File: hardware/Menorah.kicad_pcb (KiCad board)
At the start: 2 copper layers, 111.6 x 130.3 mm, 32 parts, among them J1 Conn_02x03_Odd_Even, SW1 SW_Push, U1 ATtiny85-20PU

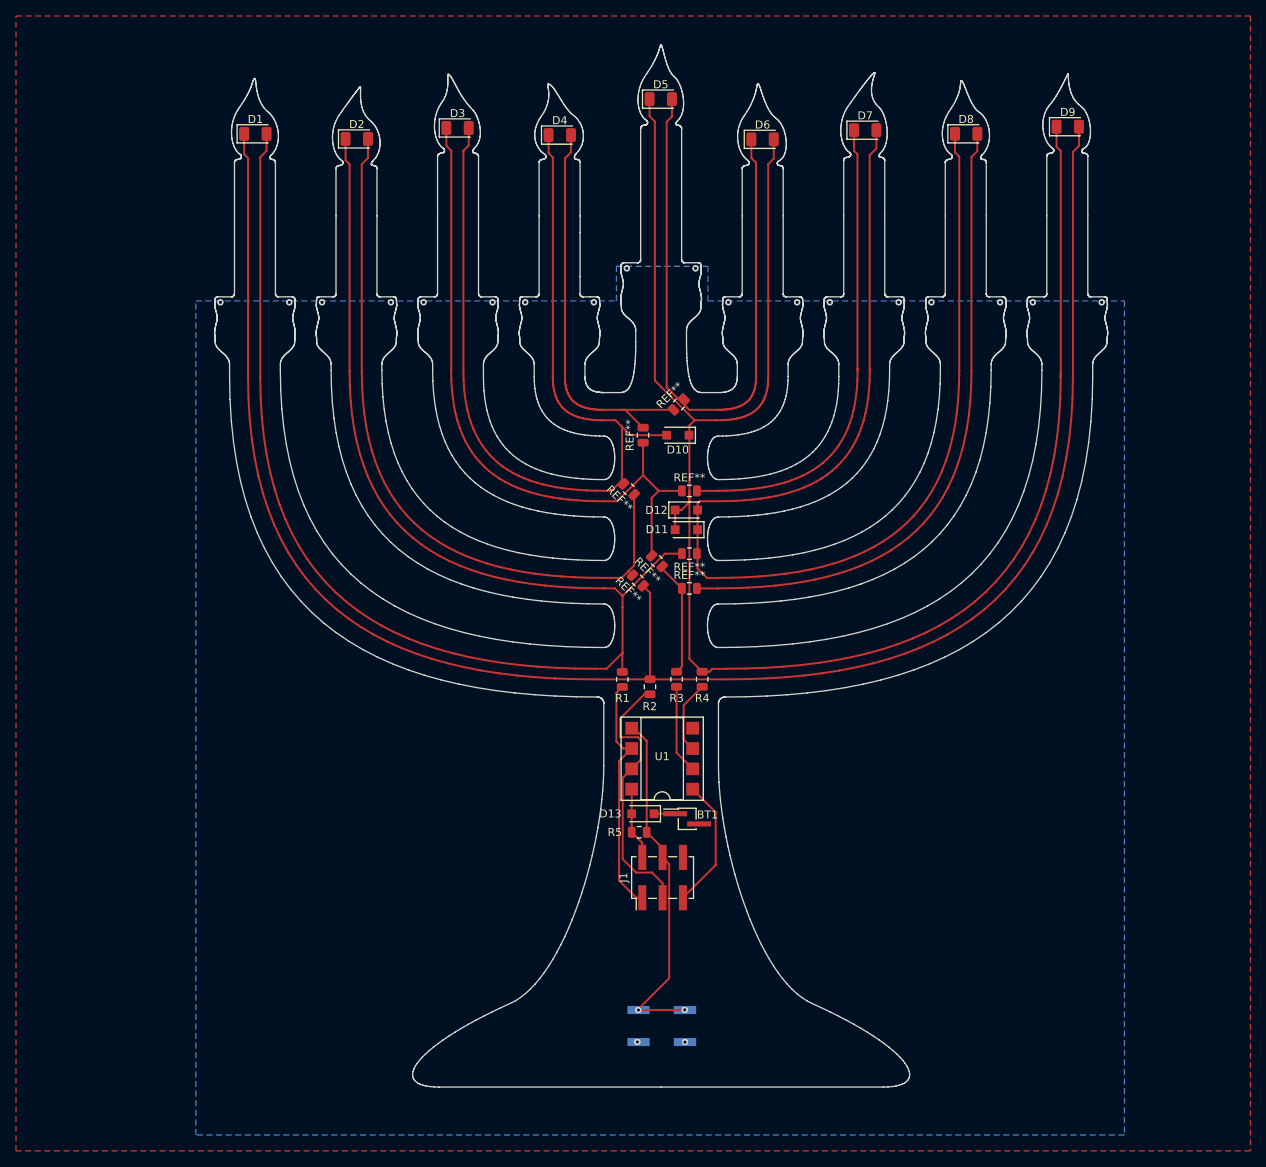
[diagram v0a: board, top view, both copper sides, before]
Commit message: Finished (?) layout, ordered boards.
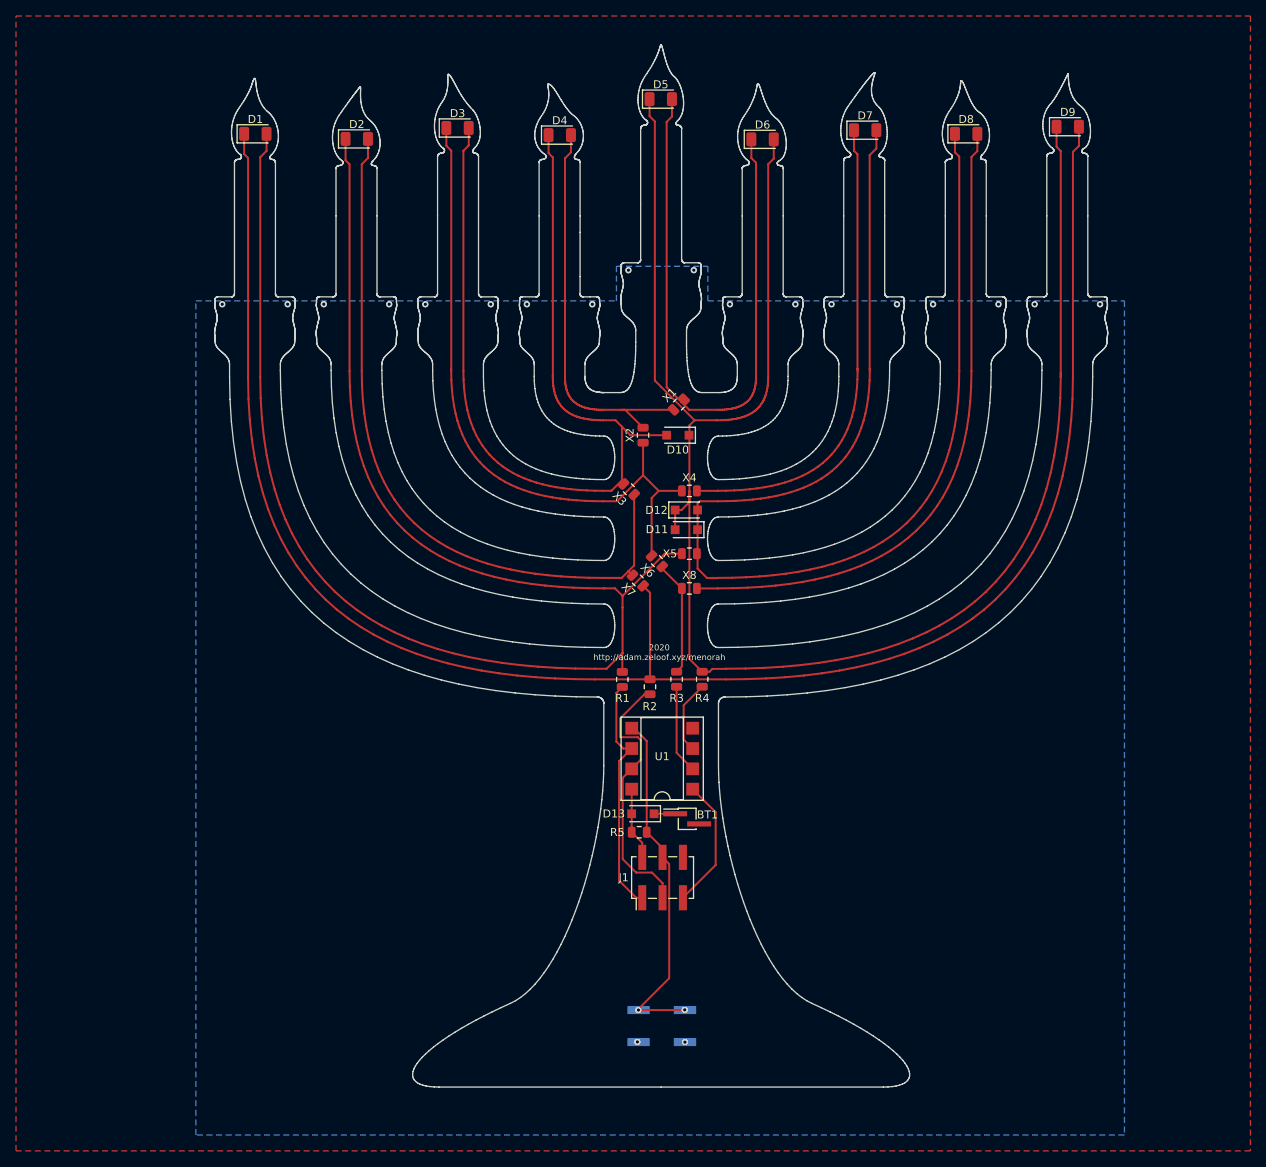
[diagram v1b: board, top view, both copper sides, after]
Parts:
- moved G*** 0.05 mm to (142.0, 103.9)
- renumbered REF** to X1, REF** to X2, REF** to X3, REF** to X4, REF** to X5, REF** to X6, REF** to X7, REF** to X8
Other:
- board text added: "2020 http://adam.zeloof.xyz/menorah"
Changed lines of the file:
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@@
   (general
     (thickness 1.6)
-    (drawings 6629)
+    (drawings 6630)
     (tracks 216)
     (zones 0)
@@
     (44 Edge.Cuts user)
     (45 Margin user)
-    (46 B.CrtYd user hide)
-    (47 F.CrtYd user hide)
-    (48 B.Fab user hide)
-    (49 F.Fab user hide)
+    (46 B.CrtYd user)
+    (47 F.CrtYd user)
+    (48 B.Fab user)
+    (49 F.Fab user)
   )
   (setup
@@
     (pcbplotparams
       (layerselection 0x010fc_ffffffff)
-      (usegerberextensions false)
+      (usegerberextensions true)
       (usegerberattributes false)
       (usegerberadvancedattributes false)
@@
       (outputformat 1)
       (mirror false)
-      (drillshape 1)
+      (drillshape 0)
       (scaleselection 1)
-      (outputdirectory ""))
+      (outputdirectory "gerbers/"))
   )
   (net 0 "")
@@
     (tags resistor)
     (attr smd)
-    (fp_text reference REF** (at 0 -1.65 135) (layer F.SilkS)
+    (fp_text reference X6 (at 0 -1.65 135) (layer F.SilkS)
       (effects (font (size 1 1) (thickness 0.15)))
     )
@@
       (effects (font (size 1 1) (thickness 0.15)))
     )
-    (fp_text user %R (at 0 0 135) (layer F.Fab)
+    (fp_text user 0 (at 0 0 135) (layer F.Fab)
       (effects (font (size 0.5 0.5) (thickness 0.08)))
     )
@@
     (tags resistor)
     (attr smd)
-    (fp_text reference REF** (at 0 -1.65) (layer F.SilkS)
+    (fp_text reference X8 (at 0 -1.65) (layer F.SilkS)
       (effects (font (size 1 1) (thickness 0.15)))
     )
@@
       (effects (font (size 1 1) (thickness 0.15)))
     )
-    (fp_text user %R (at 0 0) (layer F.Fab)
+    (fp_text user 0 (at 0 0) (layer F.Fab)
       (effects (font (size 0.5 0.5) (thickness 0.08)))
     )
@@
     (tags resistor)
     (attr smd)
-    (fp_text reference REF** (at 0 -1.65 135) (layer F.SilkS)
+    (fp_text reference X7 (at 0 -1.65 135) (layer F.SilkS)
       (effects (font (size 1 1) (thickness 0.15)))
     )
@@
       (effects (font (size 1 1) (thickness 0.15)))
     )
-    (fp_text user %R (at 0 0 135) (layer F.Fab)
+    (fp_text user 0 (at 0 0 135) (layer F.Fab)
       (effects (font (size 0.5 0.5) (thickness 0.08)))
     )
@@
     (tags resistor)
     (attr smd)
-    (fp_text reference REF** (at 0 -1.65 135) (layer F.SilkS)
+    (fp_text reference X3 (at 0 -1.65 135) (layer F.SilkS)
       (effects (font (size 1 1) (thickness 0.15)))
     )
@@
       (effects (font (size 1 1) (thickness 0.15)))
     )
-    (fp_text user %R (at 0 0 135) (layer F.Fab)
+    (fp_text user 0 (at 0 0 135) (layer F.Fab)
       (effects (font (size 0.5 0.5) (thickness 0.08)))
     )
@@
     (tags resistor)
     (attr smd)
-    (fp_text reference REF** (at 0 -1.65) (layer F.SilkS)
+    (fp_text reference X4 (at 0 -1.65) (layer F.SilkS)
       (effects (font (size 1 1) (thickness 0.15)))
     )
@@
       (effects (font (size 1 1) (thickness 0.15)))
     )
-    (fp_text user %R (at 0 0) (layer F.Fab)
+    (fp_text user 0 (at 0 0) (layer F.Fab)
       (effects (font (size 0.5 0.5) (thickness 0.08)))
     )
@@
     (tags resistor)
     (attr smd)
-    (fp_text reference REF** (at 0 -1.65 90) (layer F.SilkS)
+    (fp_text reference X2 (at 0 -1.65 90) (layer F.SilkS)
       (effects (font (size 1 1) (thickness 0.15)))
     )
@@
       (effects (font (size 1 1) (thickness 0.15)))
     )
-    (fp_text user %R (at 0 0 90) (layer F.Fab)
+    (fp_text user 0 (at 0 0 90) (layer F.Fab)
       (effects (font (size 0.5 0.5) (thickness 0.08)))
     )
@@
     (tags resistor)
     (attr smd)
-    (fp_text reference REF** (at 0 -1.65 45) (layer F.SilkS)
+    (fp_text reference X1 (at 0 -1.65 45) (layer F.SilkS)
       (effects (font (size 1 1) (thickness 0.15)))
     )
@@
       (effects (font (size 1 1) (thickness 0.15)))
     )
-    (fp_text user %R (at 0 0 45) (layer F.Fab)
+    (fp_text user 0 (at 0 0 45) (layer F.Fab)
       (effects (font (size 0.5 0.5) (thickness 0.08)))
     )
@@
     (tags resistor)
     (attr smd)
-    (fp_text reference REF** (at 0 -1.65) (layer F.SilkS)
+    (fp_text reference X5 (at 2.4384 0.00508) (layer F.SilkS)
       (effects (font (size 1 1) (thickness 0.15)))
     )
@@
       (effects (font (size 1 1) (thickness 0.15)))
     )
-    (fp_text user %R (at 0 0) (layer F.Fab)
+    (fp_text user 0 (at 0 0) (layer F.Fab)
       (effects (font (size 0.5 0.5) (thickness 0.08)))
     )
@@
   )
   (module menorah:menorah_mask (layer F.Cu)
-    (at 142.0368 103.9368)
+    (at 141.986 103.9368)
     (fp_text reference G*** (at 0 0) (layer F.SilkS) hide
       (effects (font (size 1.524 1.524) (thickness 0.3)))
@@
     (tags "Surface mounted pin header SMD 2x03 2.54mm double row")
     (attr smd)
-    (fp_text reference J1 (at 0 -4.87 270) (layer F.SilkS)
+    (fp_text reference J1 (at 0 -4.87) (layer F.SilkS)
       (effects (font (size 1 1) (thickness 0.15)))
     )
@@
     (tags resistor)
     (attr smd)
-    (fp_text reference R5 (at 3.048 0) (layer F.SilkS)
+    (fp_text reference R5 (at 2.7432 0) (layer F.SilkS)
       (effects (font (size 1 1) (thickness 0.15)))
     )
@@
     (tags D_SOD-123F)
     (attr smd)
-    (fp_text reference D13 (at 4.064 0) (layer F.SilkS)
+    (fp_text reference D13 (at 3.6322 0) (layer F.SilkS)
       (effects (font (size 1 1) (thickness 0.15)))
     )
@@
     )
   )
+  (gr_text "2020\nhttp://adam.zeloof.xyz/menorah" (at 141.732 97.409) (layer F.SilkS)
+    (effects (font (size 0.75 0.75) (thickness 0.15)))
+  )
   (gr_line (start 173.482 136.398) (end 110.998 136.398) (layer Dwgs.User) (width 0.15))
   (gr_line (start 173.228 151.892) (end 173.228 136.398) (layer Dwgs.User) (width 0.15))
@@
   (gr_line (start 190.537495 35.025657) (end 190.517148 35.027254) (layer Edge.Cuts) (width 0.05))
   (gr_line (start 190.558124 35.025118) (end 190.537495 35.025657) (layer Edge.Cuts) (width 0.05))
-  (via (at 184.3278 53.6448) (size 0.8) (drill 0.4) (layers F.Cu B.Cu) (net 1))
-  (via (at 133.5532 53.6448) (size 0.8) (drill 0.4) (layers F.Cu B.Cu) (net 1))
-  (via (at 120.8786 53.6448) (size 0.8) (drill 0.4) (layers F.Cu B.Cu) (net 1))
-  (via (at 108.1786 53.6448) (size 0.8) (drill 0.4) (layers F.Cu B.Cu) (net 1))
+  (via (at 184.1246 53.88864) (size 0.8) (drill 0.4) (layers F.Cu B.Cu) (net 1))
+  (via (at 133.35254 53.89118) (size 0.8) (drill 0.4) (layers F.Cu B.Cu) (net 1))
+  (via (at 120.66016 53.88864) (size 0.8) (drill 0.4) (layers F.Cu B.Cu) (net 1))
+  (via (at 107.9627 53.8861) (size 0.8) (drill 0.4) (layers F.Cu B.Cu) (net 1))
   (via (at 138.9888 146.1008) (size 0.8) (drill 0.4) (layers F.Cu B.Cu) (net 1))
   (via (at 144.9324 146.1262) (size 0.8) (drill 0.4) (layers F.Cu B.Cu) (net 1))
-  (via (at 95.4786 53.6448) (size 0.8) (drill 0.4) (layers F.Cu B.Cu) (net 1))
-  (via (at 86.868 53.6448) (size 0.8) (drill 0.4) (layers F.Cu B.Cu) (net 1))
-  (via (at 99.568 53.6448) (size 0.8) (drill 0.4) (layers F.Cu B.Cu) (net 1))
-  (via (at 112.268 53.6448) (size 0.8) (drill 0.4) (layers F.Cu B.Cu) (net 1))
-  (via (at 124.968 53.6448) (size 0.8) (drill 0.4) (layers F.Cu B.Cu) (net 1))
-  (via (at 137.668 49.403) (size 0.8) (drill 0.4) (layers F.Cu B.Cu) (net 1))
-  (via (at 146.2532 49.403) (size 0.8) (drill 0.4) (layers F.Cu B.Cu) (net 1))
-  (via (at 150.368 53.6448) (size 0.8) (drill 0.4) (layers F.Cu B.Cu) (net 1))
-  (via (at 158.9532 53.6448) (size 0.8) (drill 0.4) (layers F.Cu B.Cu) (net 1))
-  (via (at 163.0426 53.6448) (size 0.8) (drill 0.4) (layers F.Cu B.Cu) (net 1))
-  (via (at 171.6532 53.6448) (size 0.8) (drill 0.4) (layers F.Cu B.Cu) (net 1))
-  (via (at 175.7426 53.6448) (size 0.8) (drill 0.4) (layers F.Cu B.Cu) (net 1))
-  (via (at 188.4172 53.6448) (size 0.8) (drill 0.4) (layers F.Cu B.Cu) (net 1))
-  (via (at 197.0278 53.6448) (size 0.8) (drill 0.4) (layers F.Cu B.Cu) (net 1))
+  (via (at 95.27286 53.8861) (size 0.8) (drill 0.4) (layers F.Cu B.Cu) (net 1))
+  (via (at 87.0966 53.88864) (size 0.8) (drill 0.4) (layers F.Cu B.Cu) (net 1))
+  (via (at 99.79152 53.8861) (size 0.8) (drill 0.4) (layers F.Cu B.Cu) (net 1))
+  (via (at 112.48136 53.89118) (size 0.8) (drill 0.4) (layers F.Cu B.Cu) (net 1))
+  (via (at 125.17628 53.8861) (size 0.8) (drill 0.4) (layers F.Cu B.Cu) (net 1))
+  (via (at 137.86866 49.62906) (size 0.8) (drill 0.4) (layers F.Cu B.Cu) (net 1))
+  (via (at 146.04238 49.62652) (size 0.8) (drill 0.4) (layers F.Cu B.Cu) (net 1))
+  (via (at 150.55342 53.8861) (size 0.8) (drill 0.4) (layers F.Cu B.Cu) (net 1))
+  (via (at 158.73984 53.89118) (size 0.8) (drill 0.4) (layers F.Cu B.Cu) (net 1))
+  (via (at 163.25596 53.8861) (size 0.8) (drill 0.4) (layers F.Cu B.Cu) (net 1))
+  (via (at 171.43476 53.8861) (size 0.8) (drill 0.4) (layers F.Cu B.Cu) (net 1))
+  (via (at 175.95088 53.89118) (size 0.8) (drill 0.4) (layers F.Cu B.Cu) (net 1))
+  (via (at 188.6458 53.88864) (size 0.8) (drill 0.4) (layers F.Cu B.Cu) (net 1))
+  (via (at 196.81952 53.8861) (size 0.8) (drill 0.4) (layers F.Cu B.Cu) (net 1))
   (segment (start 143.7118 117.5766) (end 141.0746 117.5766) (width 0.25) (layer F.Cu) (net 2))
   (segment (start 92.6368 34.7188) (end 92.6368 32.5882) (width 0.25) (layer F.Cu) (net 3))
